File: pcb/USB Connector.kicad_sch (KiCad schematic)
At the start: 14 parts, among them J1 USB_C_Receptacle_USB2.0, U1 FT230XQ

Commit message: Completed schematic oranization and components connection
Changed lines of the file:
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@@
   (junction (at 115.57 71.12) (diameter 0) (color 0 0 0 0)
+  )
+  (junction (at 176.53 52.07) (diameter 0) (color 0 0 0 0)
   )
   (junction (at 146.05 153.67) (diameter 0) (color 0 0 0 0)
@@
     (stroke (width 0) (type default))
   )
+  (wire (pts (xy 176.53 50.8) (xy 176.53 52.07))
+    (stroke (width 0) (type default))
+  )
   (wire (pts (xy 114.3 134.62) (xy 92.71 134.62))
     (stroke (width 0) (type default))
@@
     (stroke (width 0) (type default))
   )
-  (wire (pts (xy 166.37 52.07) (xy 171.45 52.07))
+  (wire (pts (xy 166.37 52.07) (xy 176.53 52.07))
     (stroke (width 0) (type default))
   )
@@
   )
   (wire (pts (xy 114.3 52.07) (xy 153.67 52.07))
+    (stroke (width 0) (type default))
+  )
+  (wire (pts (xy 176.53 52.07) (xy 180.34 52.07))
     (stroke (width 0) (type default))
   )
@@
     (effects (font (size 1.27 1.27)) (justify right bottom))
   )
-  (hierarchical_label "5V_USB" (shape output) (at 171.45 52.07 0) (fields_autoplaced)
+  (hierarchical_label "5V_USB" (shape output) (at 180.34 52.07 0) (fields_autoplaced)
     (effects (font (size 1.27 1.27)) (justify left))
   )
@@
         )
       )
+    )
+  )
+  (symbol (lib_id "power:PWR_FLAG") (at 176.53 50.8 0) (unit 1)
+    (in_bom yes) (on_board yes) (dnp no) (fields_autoplaced)
+    (property "Reference" "#FLG02" (at 176.53 48.895 0)
+      (effects (font (size 1.27 1.27)) hide)
+    )
+    (property "Value" "PWR_FLAG" (at 176.53 46.99 0)
+      (effects (font (size 1.27 1.27)))
+    )
+    (property "Footprint" "" (at 176.53 50.8 0)
+      (effects (font (size 1.27 1.27)) hide)
+    )
+    (property "Datasheet" "~" (at 176.53 50.8 0)
+      (effects (font (size 1.27 1.27)) hide)
+    )
+    (pin "1")
+    (instances
+      (project "Signal Generator"
+        (path "/f6255c48-6253-4c69-a6db-1ceaf4eff04d/9d99cf62-f968-426c-bcde-130807203ad1"
+          (reference "#FLG02") (unit 1)
+        )
+      )

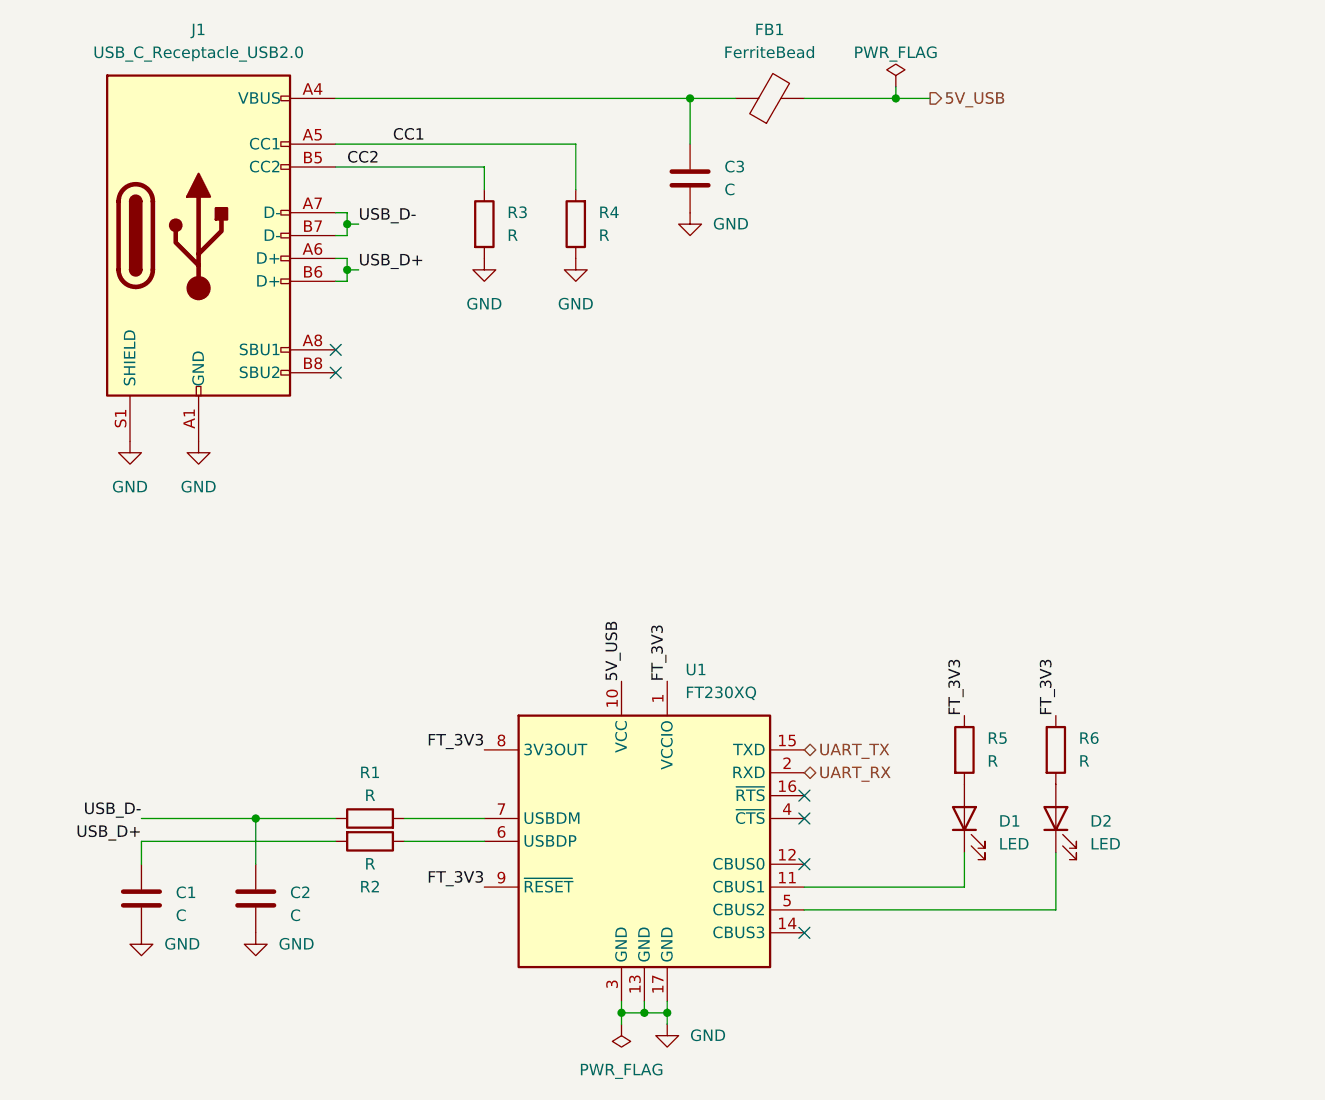
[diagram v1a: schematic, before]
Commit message: Added micro SD and RGB led to schematic. Also added components part numbers
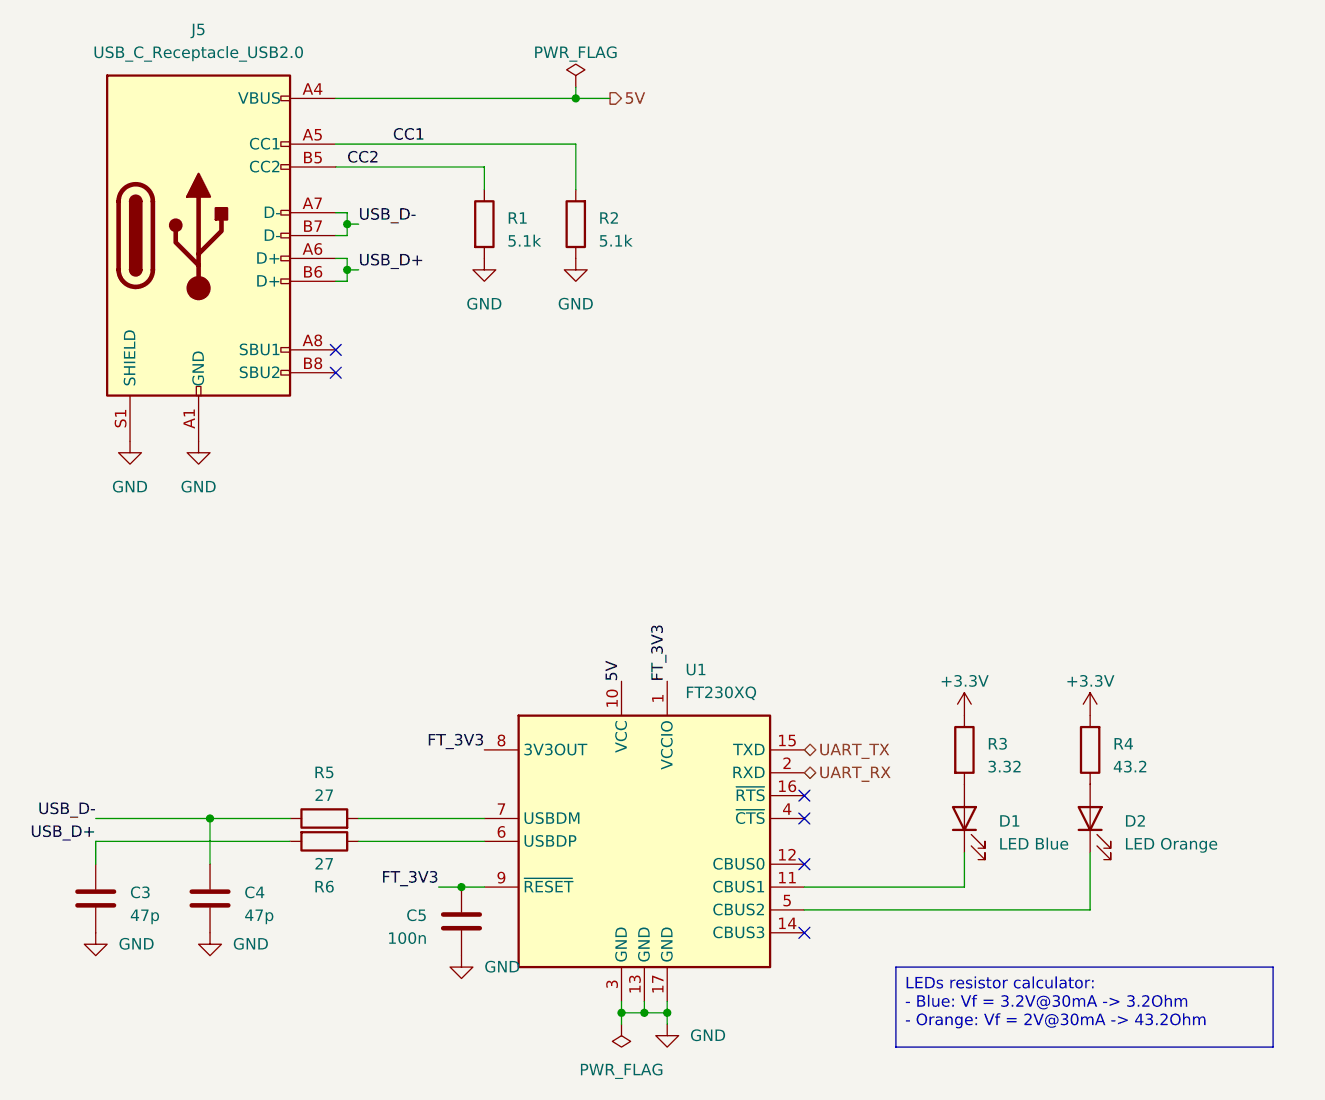
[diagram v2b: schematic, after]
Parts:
- removed C3: C, Capacitor_SMD:C_0603_1608Metric, symbol Device:C
- removed FB1: FerriteBead, Resistor_SMD:R_0805_2012Metric, symbol Device:FerriteBead
- added C5: 100n, Capacitor_SMD:C_0603_1608Metric, symbol Device:C
- C3: renamed from C1; value C -> 47p; PN (none) -> GQM1875C2E470JB12D
- C4: renamed from C2; value C -> 47p; PN (none) -> GQM1875C2E470JB12D
- D1: value LED -> LED Blue; PN (none) -> 150060BS75000
- D2: value LED -> LED Orange; PN (none) -> 150060AS75000
- J5: renamed from J1; footprint Skyward library:USB4105-GF-A -> Signal Generator Components:USB4105-GF-A; PN (none) -> USB4105-GF-A-120
- R1: renamed from R3; value R -> 5.1k; PN (none) -> ERJ-3EKF5101V
- R2: renamed from R4; value R -> 5.1k; PN (none) -> ERJ-3EKF5101V
- R3: renamed from R5; value R -> 3.32; PN (none) -> RC0603FR-073R32L
- R4: renamed from R6; value R -> 43.2; PN (none) -> RT0603FRE0743R2L
- R5: renamed from R1; value R -> 27; PN (none) -> ERJ-3RED27R0V
- R6: renamed from R2; value R -> 27; PN (none) -> ERJ-3RED27R0V
- U1: PN (none) -> FT230XQ-T
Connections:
- net 5V_USB is gone; now on net 5V: U1.10 (VCC)
- net FT_3V3: now also C5.1; no longer R3.1, R4.1
- net GND: now also C5.2
- net 5V: now reaches J5.A4 (VBUS), J5.A9 (VBUS), J5.B4 (VBUS), J5.B9 (VBUS)
- net at D2.2 (A): now also R4.1; no longer R4.2
- new net +3.3V: R3.1, R4.2
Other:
- moved on the sheet: C3, C4, D2, R4, R5, R6

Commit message: Completed schematic and tried some simulations
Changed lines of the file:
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@@
   (title_block
     (title "USB Connector")
+    (date "2023-01-16")
+    (rev "0")
   )
   (junction (at 100.33 132.08) (diameter 0) (color 0 0 0 0)
@@
     (stroke (width 0) (type default))
   )
-  (text_box "LEDs resistor calculator:\n - Blue: Vf = 3.2V@30mA -> 3.2Ohm\n - Orange: Vf = 2V@30mA -> 43.2Ohm"
+  (text_box "LEDs resistor calculator:\n - Blue: Vf = 3.2V@30mA -> 3.32Ohm\n - Orange: Vf = 2V@30mA -> 43.2Ohm"
     (at 176.53 148.59 0) (size 41.91 8.89)
     (stroke (width 0) (type default))

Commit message: Added blocking capacitor to headphones jack
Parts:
- renumbered C3 to C4, C4 to C5, C5 to C6
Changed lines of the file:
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@@
   (symbol (lib_id "Device:C") (at 100.33 140.97 0) (unit 1)
     (in_bom yes) (on_board yes) (dnp no) (fields_autoplaced)
-    (property "Reference" "C4" (at 104.14 140.335 0)
+    (property "Reference" "C5" (at 104.14 140.335 0)
       (effects (font (size 1.27 1.27)) (justify left))
     )
@@
       (project "Signal Generator"
         (path "/f6255c48-6253-4c69-a6db-1ceaf4eff04d/9d99cf62-f968-426c-bcde-130807203ad1"
-          (reference "C4") (unit 1)
+          (reference "C5") (unit 1)
         )
       )
@@
   (symbol (lib_id "Device:C") (at 128.27 143.51 0) (mirror y) (unit 1)
     (in_bom yes) (on_board yes) (dnp no)
-    (property "Reference" "C5" (at 124.46 142.875 0)
+    (property "Reference" "C6" (at 124.46 142.875 0)
       (effects (font (size 1.27 1.27)) (justify left))
     )
@@
       (project "Signal Generator"
         (path "/f6255c48-6253-4c69-a6db-1ceaf4eff04d/9d99cf62-f968-426c-bcde-130807203ad1"
-          (reference "C5") (unit 1)
+          (reference "C6") (unit 1)
         )
       )
@@
   (symbol (lib_id "Device:C") (at 87.63 140.97 0) (unit 1)
     (in_bom yes) (on_board yes) (dnp no) (fields_autoplaced)
-    (property "Reference" "C3" (at 91.44 140.335 0)
+    (property "Reference" "C4" (at 91.44 140.335 0)
       (effects (font (size 1.27 1.27)) (justify left))
     )
@@
       (project "Signal Generator"
         (path "/f6255c48-6253-4c69-a6db-1ceaf4eff04d/9d99cf62-f968-426c-bcde-130807203ad1"
-          (reference "C3") (unit 1)
-        )
-      )
+          (reference "C4") (unit 1)
+        )
+      )

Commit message: Fixed FTDI connection to the stm32
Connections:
- net UART_RX renamed FTDI_RX
- net UART_TX renamed FTDI_TX
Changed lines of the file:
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@@
     (effects (font (size 1.27 1.27)) (justify left))
   )
-  (hierarchical_label "UART_TX" (shape bidirectional) (at 166.37 124.46 0) (fields_autoplaced)
+  (hierarchical_label "FTDI_TX" (shape bidirectional) (at 166.37 124.46 0) (fields_autoplaced)
     (effects (font (size 1.27 1.27)) (justify left))
   )
-  (hierarchical_label "UART_RX" (shape bidirectional) (at 166.37 127 0) (fields_autoplaced)
+  (hierarchical_label "FTDI_RX" (shape bidirectional) (at 166.37 127 0) (fields_autoplaced)
     (effects (font (size 1.27 1.27)) (justify left))
   )

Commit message: Switch to stm32f205
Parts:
- renumbered R5 to R1, R6 to R2, R1 to R3, R2 to R4, R3 to R5, R4 to R6
